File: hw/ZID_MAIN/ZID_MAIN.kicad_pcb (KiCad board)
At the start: 6 copper layers, 127 x 88.9 mm, 175 parts, among them J1 Conn 1x04 0.1" Socket, J10 FFC/FPC-40 Socket, J11 JST-PH-K B6B, J14 USB-C PWR ONLY, J15 Conn 2x03 pin hdr 0.1", J2 JST-PH-K B6B, J3 Conn 1x02 0.1" pin, J4 Conn 1x03 0.1" pin, J5 Conn 1x08 0.1" pin, J6 Conn 1x08 0.1" pin, J7 Conn 2x04 0.1" pin, J8 Conn 2x02 0.1" pin, J9 Conn 2x04 0.1" pin, M1 WS-RP2040-Zero, SW1 SW_Push, SW2 SW_DIP_x02, U1 OSC-20MHz, U10 27WZ06, U11 74LVC125AS, U12 74LVC273, U13 74FCT2245, U14 AS7C1024B, U15 ATF1508AS, U16 74FCT2245, U18 ATF1508AS, U2 74FCT2245, U20 74FCT2244, U22 ATF1504AS-44T, U23 74AHCT00, U24 74FCT2244, U3 24LC32, U4 MIC2775, U5 SST39SF010, U6 74LVC245, U7 74FCT2245, U8 74AHCT14, U9 Z80 C20MHz-PLCC

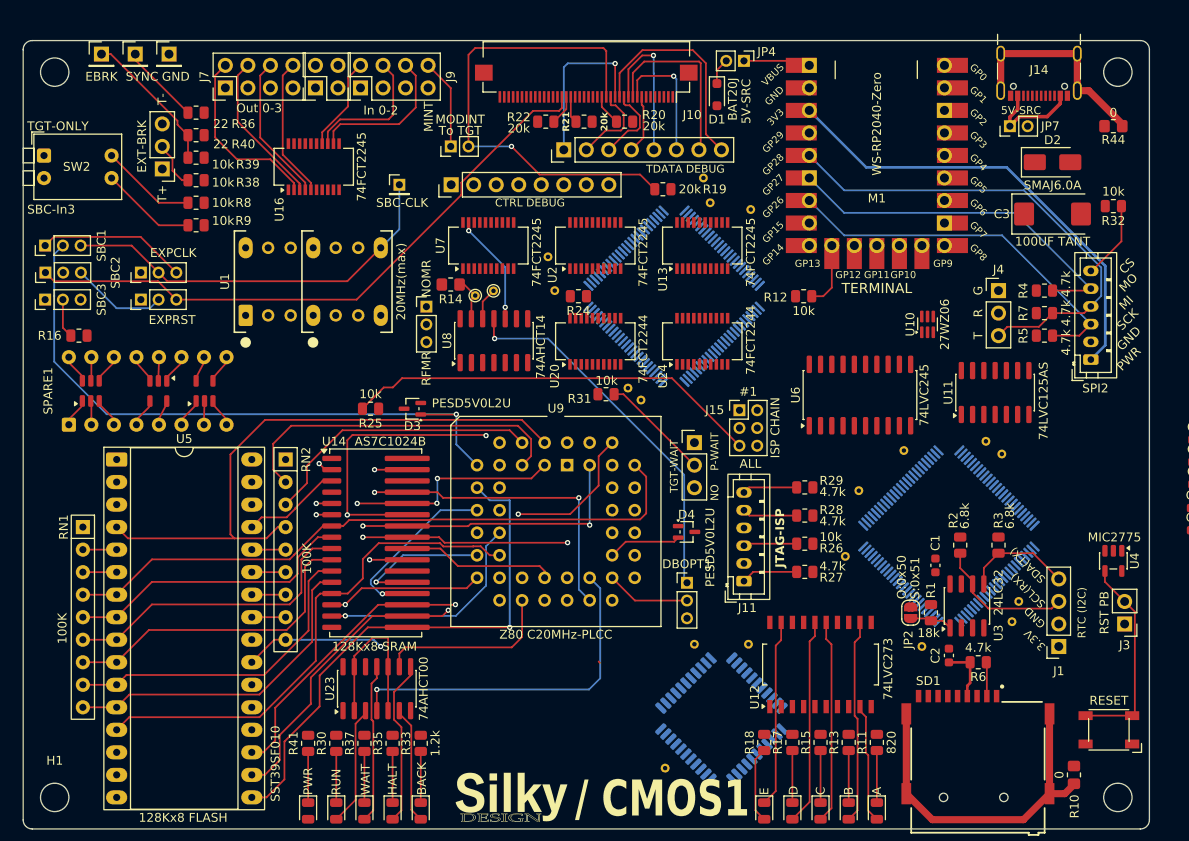
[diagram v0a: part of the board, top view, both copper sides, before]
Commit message: SCHM/PCB: Small pin assignment changes on U15.
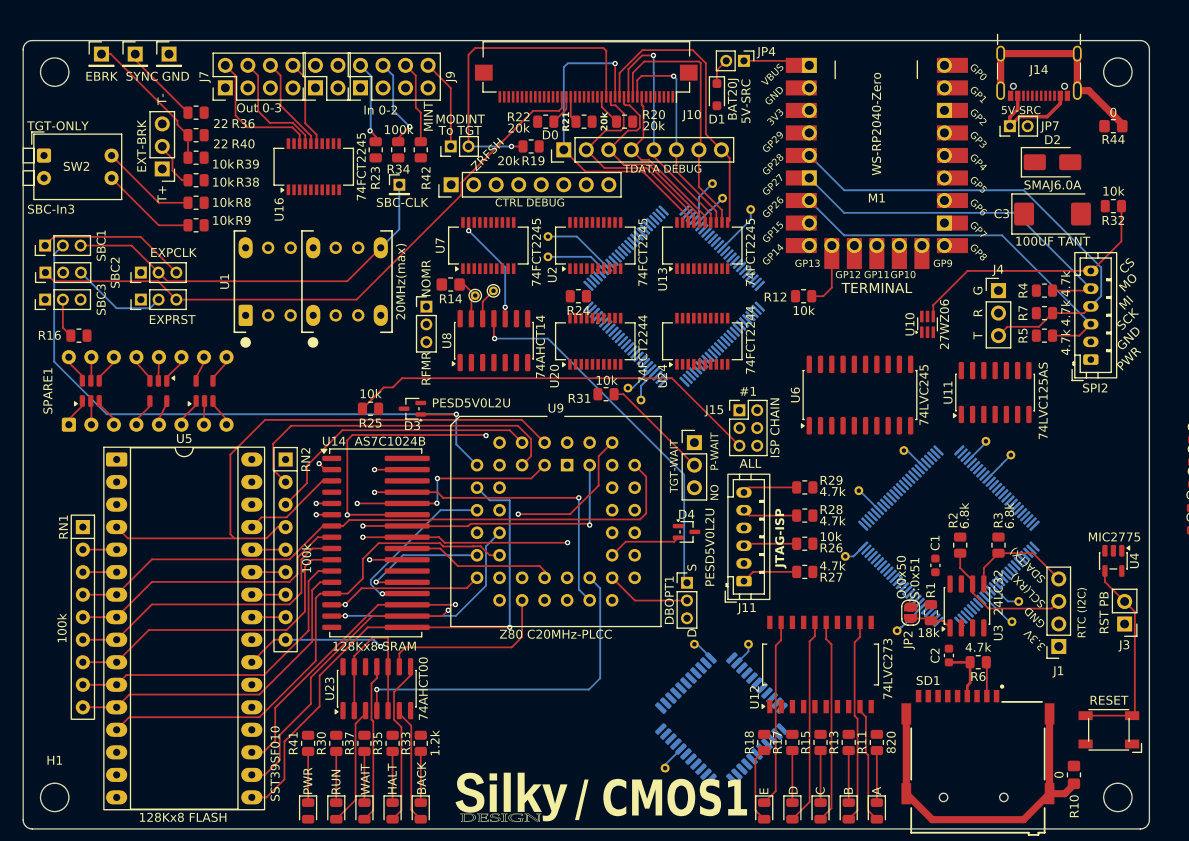
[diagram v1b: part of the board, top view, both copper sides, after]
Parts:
- added R23: 100k, Resistor_SMD:R_0805_2012Metric, F.Cu at (98.5, 68.2)
- added R34: 100k, Resistor_SMD:R_0805_2012Metric, F.Cu at (101.0, 68.2)
- added R42: 100k, Resistor_SMD:R_0805_2012Metric, F.Cu at (103.6, 68.2)
- RN1, RN2: value 100K -> 100k
- moved R19 15.6 mm to (116.0, 67.8)
- moved TP10 6.14 mm to (117.9, 78.0)
- moved TP23 3.31 mm to (157.3, 122.4)
- moved TP4 1.49 mm to (137.6, 73.7)
- moved TP5 1.20 mm to (136.5, 72.0)
- moved TP6 1.03 mm to (170.1, 102.6)
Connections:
- TP17 pad 1: Net-(U15-BMC22/IO) -> Net-(U15-BMC17/IO)
- TP19 pad 1: Net-(U15-CMC41/IO) -> Net-(U15-CMC45/IO)
- U15 pad 10: Net-(U15-BMC22/IO) -> unconnected-(U15-BMC22/IO-Pad10)
- U15 pad 14: /ZWR- -> Net-(U15-BMC17/IO)
- U15 pad 17: /ZRD- -> Net-(U15-CMC45/IO)
- U15 pad 20: Net-(U15-CMC41/IO) -> unconnected-(U15-CMC41/IO-Pad20)
- U15 pad 88: unconnected-(U15-IN/OE1-Pad88) -> /ZRD-
- U15 pad 89: unconnected-(U15-IN/GCLR-Pad89) -> /LRST-
- U15 pad 90: unconnected-(U15-IN/OE2/GCK2-Pad90) -> /ZWR-
- U16 pad 11: /ZM1- -> /TM1-
- U16 pad 12: /SBC_I2 -> /SBC_GPI2
- U16 pad 13: /SBC_I1 -> /SBC_GPI1
- U16 pad 14: /SBC_I0 -> /SBC_GPI0
- U16 pad 15: /SBC_GPO3 -> /SBC_O3
- U16 pad 16: /SBC_GPO2 -> /SBC_O2
- U16 pad 17: /SBC_GPO1 -> /SBC_O1
- U16 pad 18: /SBC_GPO0 -> /SBC_O0
- U16 pad 2: /SBC_O0 -> /SBC_GPO0
- U16 pad 3: /SBC_O1 -> /SBC_GPO1
- U16 pad 4: /SBC_O2 -> /SBC_GPO2
- U16 pad 5: /SBC_O3 -> /SBC_GPO3
- U16 pad 6: /SBC_GPI0 -> /SBC_I0
- U16 pad 7: /SBC_GPI1 -> /SBC_I1
- U16 pad 8: /SBC_GPI2 -> /SBC_I2
- U16 pad 9: /TM1- -> /ZM1-
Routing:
- net /ZA0: track 102.6 -> 37.3 mm
- net +3.3V: track 58.2 -> 6.34 mm
- net /SPICS2-: track 8.80 -> 29.3 mm
- net /TD0: track 19.0 -> 36.8 mm
- net /TINT-: track 54.5 -> 37.7 mm
- net /TD1: track 9.63 -> 25.6 mm
- net /TD2: track 9.02 -> 23.1 mm
- net /TD3: track 6.61 -> 18.8 mm
- net /TD4: track 17.2 -> 28.1 mm
- net /TD5: track 14.6 -> 24.7 mm
- net /TD6: track 20.8 -> 29.8 mm
- net /TD7: track 24.6 -> 33.3 mm
- net Net-(U18-FMC89/IO): track 0.00 -> 8.11 mm
- net /SBC_I2: track 17.0 -> 9.32 mm
- net Net-(U18-FMC88/IO): track 0.00 -> 6.95 mm
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
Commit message: PCB: AB+PCL pinout. Exp-BP add position.
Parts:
- moved TP19 10.7 mm to (160.2, 125.2)
- moved TP17 6.65 mm to (175.6, 114.3)
- moved TP6 6.03 mm to (174.1, 107.2)
- moved TP25 3.25 mm to (153.1, 116.8)
- moved TP23 1.20 mm to (156.7, 121.4)
- moved TP21 1.02 mm to (157.0, 102.2)
- moved TP24 0.53 mm to (152.7, 106.2)
- moved TP18 0.28 mm to (167.6, 101.1)
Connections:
- TP17 pad 1: Net-(U15-BMC17/IO) -> Net-(U15-BMC30/IO)
- TP19 pad 1: Net-(U15-CMC45/IO) -> Net-(U15-CMC33/IO)
- TP21 pad 1: Net-(U15-GMC107/IO) -> Net-(U15-GMC104/IO)
- TP23 pad 1: Net-(U15-DMC57/IO) -> Net-(U15-DMC54/IO)
- TP25 pad 1: Net-(U15-EMC80/IO) -> Net-(U15-EMC72/IO)
- TP6 pad 1: Net-(U15-H128/IO/GCK3) -> Net-(U15-AMC9/IO)
- U15 pad 1: /ZD2 -> /ZA5
- U15 pad 10: unconnected-(U15-BMC22/IO-Pad10) -> /ZA9
- U15 pad 100: /ZD1 -> /ZA4
- U15 pad 13: unconnected-(U15-BMC19/IO-Pad13) -> /ZA13
- U15 pad 14: Net-(U15-BMC17/IO) -> unconnected-(U15-BMC17/IO-Pad14)
- U15 pad 16: unconnected-(U15-CMC46/IO-Pad16) -> /ZD7
- U15 pad 17: Net-(U15-CMC45/IO) -> /ZD6
- U15 pad 19: unconnected-(U15-CMC43/IO-Pad19) -> /ZD5
- U15 pad 2: /ZD0 -> /ZA6
- U15 pad 20: unconnected-(U15-CMC41/IO-Pad20) -> /ZD4
- U15 pad 21: unconnected-(U15-CMC40/IO-Pad21) -> /ZD3
- U15 pad 22: unconnected-(U15-CMC38/IO-Pad22) -> /ZD2
- U15 pad 23: unconnected-(U15-CMC37/IO-Pad23) -> /ZD1
- U15 pad 24: unconnected-(U15-CMC35/IO-Pad24) -> /ZD0
- U15 pad 25: unconnected-(U15-CMC33/IO-Pad25) -> Net-(U15-CMC33/IO)
- U15 pad 28: /ZA9 -> /ZID_IO
- U15 pad 31: Net-(U15-DMC57/IO) -> unconnected-(U15-DMC57/IO-Pad31)
- U15 pad 33: unconnected-(U15-DMC54/IO-Pad33) -> Net-(U15-DMC54/IO)
- U15 pad 40: /ZA10 -> unconnected-(U15-EMC65/IO-Pad40)
- U15 pad 41: /ZA11 -> unconnected-(U15-E67/IO/PD2-Pad41)
- U15 pad 42: /ZA12 -> unconnected-(U15-EMC69/IO-Pad42)
- U15 pad 44: /ZA13 -> unconnected-(U15-EMC70/IO-Pad44)
- U15 pad 45: /ZA14 -> Net-(U15-EMC72/IO)
- U15 pad 47: /ZA8 -> /ZA12
- U15 pad 48: /ZA4 -> unconnected-(U15-EMC77/IO-Pad48)
- U15 pad 49: /ZA5 -> /ZA14
- U15 pad 5: /ZA3 -> Net-(U15-BMC30/IO)
- U15 pad 50: Net-(U15-EMC80/IO) -> unconnected-(U15-EMC80/IO-Pad50)
- U15 pad 52: /ZA6 -> unconnected-(U15-FMC81/IO-Pad52)
- U15 pad 53: /ZA7 -> unconnected-(U15-FMC83/IO-Pad53)
- U15 pad 57: unconnected-(U15-FMC89/IO-Pad57) -> /ZA10
- U15 pad 60: unconnected-(U15-FMC93/IO-Pad60) -> /ZA8
- U15 pad 68: /ZID_IO -> Net-(U15-GMC104/IO)
- U15 pad 7: /BRKN_AEQ -> /ZA1
- U15 pad 70: Net-(U15-GMC107/IO) -> unconnected-(U15-GMC107/IO-Pad70)
- U15 pad 8: /BRK1_AEQ -> unconnected-(U15-BMC25/IO-Pad8)
- U15 pad 85: Net-(U15-H128/IO/GCK3) -> unconnected-(U15-H128/IO/GCK3-Pad85)
- U15 pad 9: unconnected-(U15-BMC24/IO-Pad9) -> /ZA3
- U15 pad 92: /ZD7 -> /BRKN_AEQ
- U15 pad 93: /ZA1 -> /BRK1_AEQ
- U15 pad 94: /ZA0 -> unconnected-(U15-AMC13/IO-Pad94)
- U15 pad 96: /ZD6 -> /ZA0
- U15 pad 97: /ZD4 -> Net-(U15-AMC9/IO)
- U15 pad 98: /ZD5 -> /ZA11
- U15 pad 99: /ZD3 -> /ZA7
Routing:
- net Net-(U15-BMC30/IO): track 0.00 -> 5.76 mm
- net Net-(U15-CMC33/IO): track 0.00 -> 5.67 mm
- net Net-(U15-CMC45/IO): track 4.28 -> 0.00 mm
- net Net-(U15-DMC57/IO): track 4.09 -> 0.00 mm
- net Net-(U15-DMC54/IO): track 0.00 -> 3.85 mm
- net Net-(U15-H128/IO/GCK3): track 3.75 -> 0.00 mm
- net Net-(U15-BMC17/IO): track 3.47 -> 0.00 mm
- net Net-(U15-GMC104/IO): track 0.00 -> 3.41 mm
- net Net-(U15-AMC9/IO): track 0.00 -> 3.30 mm
- net Net-(U15-EMC72/IO): track 0.00 -> 3.02 mm
- net Net-(U15-GMC107/IO): track 2.49 -> 0.00 mm
- net Net-(U15-EMC80/IO): track 2.48 -> 0.00 mm
- net Net-(U15-FMC88/IO): track 3.09 -> 3.69 mm

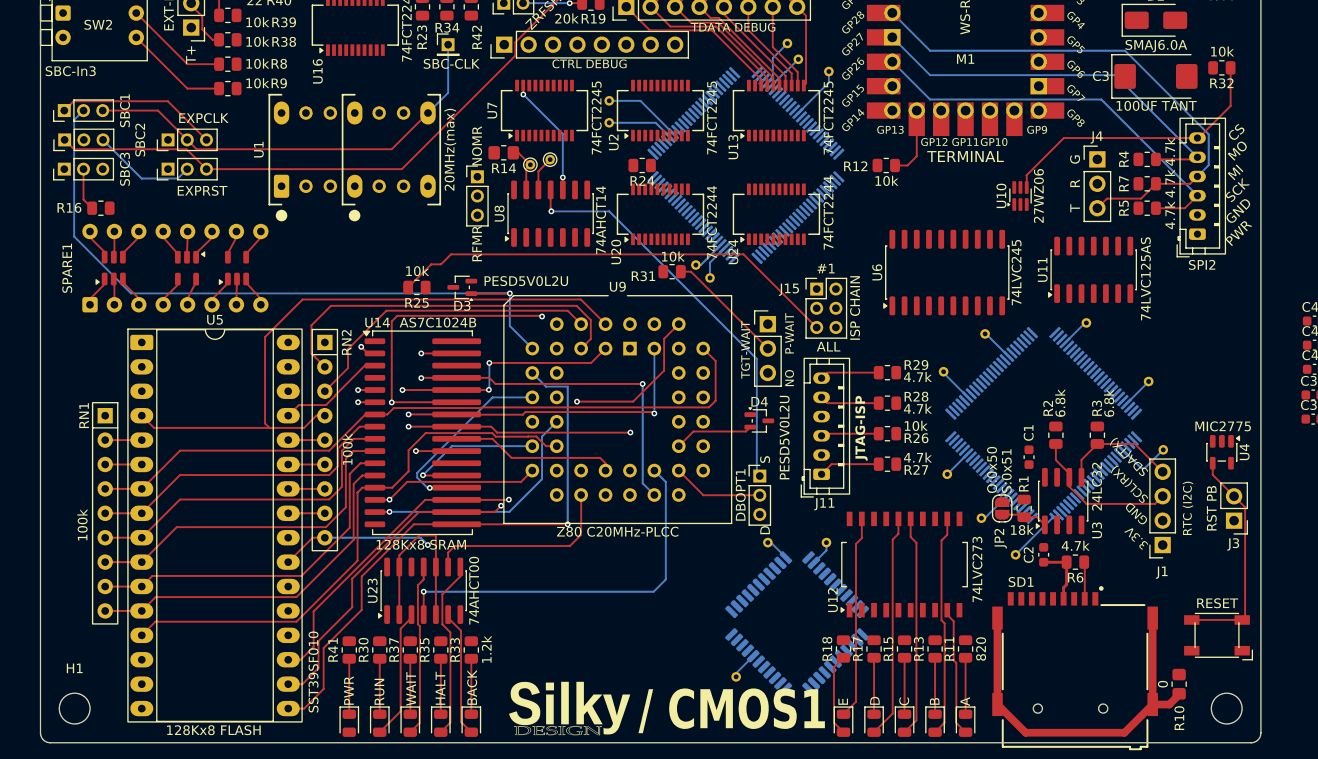
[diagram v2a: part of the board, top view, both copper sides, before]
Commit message: PCB layout progress before SRAM move. PLD: Allow upper-8 address only on BRK1.
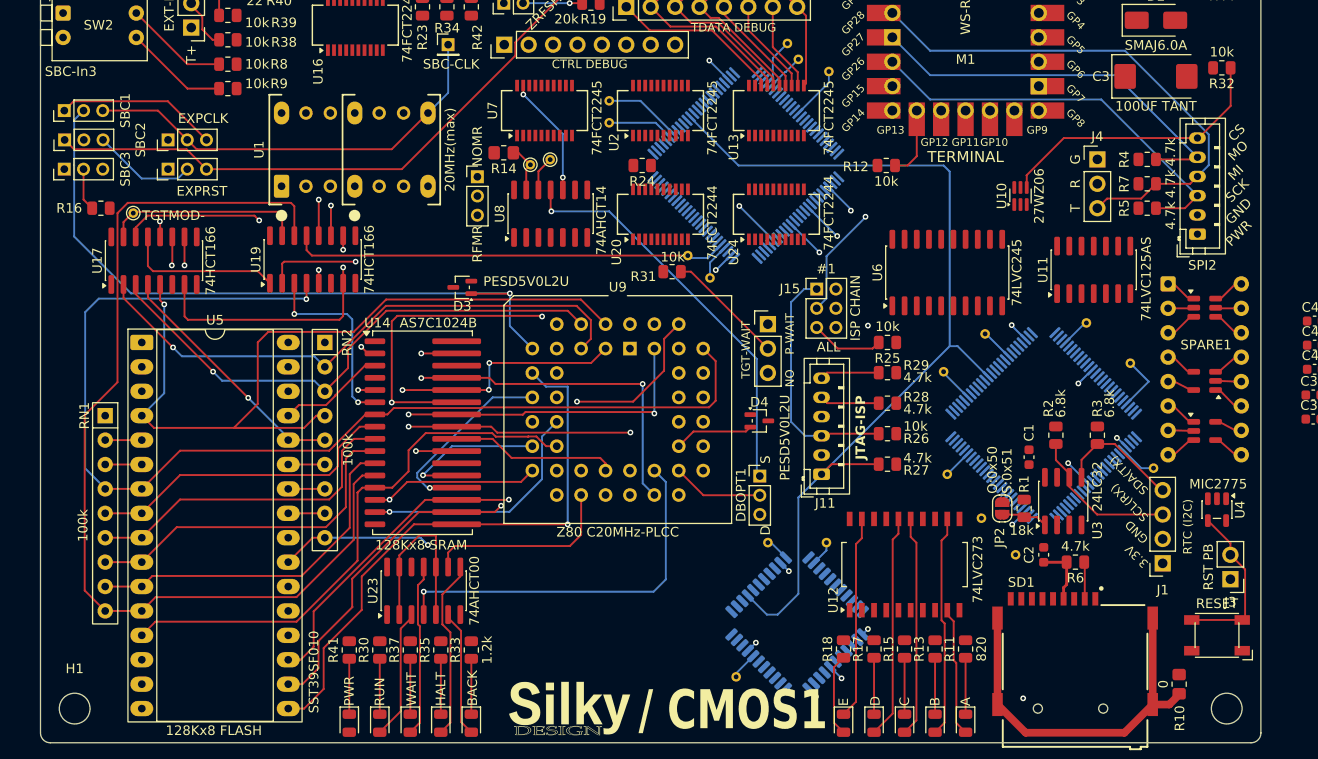
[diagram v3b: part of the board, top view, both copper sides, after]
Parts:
- added TP12: TestPoint, TestPoint:TestPoint_THTPad_D1.0mm_Drill0.5mm, F.Cu at (68.4, 89.7)
- added U17: 74HCT166, Package_SO:SOIC-16_3.9x9.9mm_P1.27mm, F.Cu at (70.5, 94.6)
- added U19: 74HCT166, Package_SO:SOIC-16_3.9x9.9mm_P1.27mm, F.Cu at (87.1, 94.5)
- moved SPARE1 112.2 mm to (176.1, 97.0), turned to 0 degrees
- moved R25 49.3 mm to (146.9, 103.1)
- moved J3 6.10 mm to (182.6, 127.8)
- moved U4 5.99 mm to (181.2, 120.5)
- moved TP6 2.69 mm to (172.1, 105.3)
- moved TP17 2.16 mm to (174.6, 116.2)
- moved J1 1.91 mm to (175.5, 126.1)
- moved TP9 1.30 mm to (126.1, 94.1)
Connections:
- net /IO59 renamed /PCRD_DIN
- TP19 pad 1: Net-(U15-CMC33/IO) -> Net-(U15-DMC54/IO)
- TP23 pad 1: Net-(U15-DMC54/IO) -> Net-(U15-CMC33/IO)
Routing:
- net /PC_LATCH-: track 0.00 -> 119.5 mm, vias 0 -> 3
- net /ZID_IO: track 0.00 -> 99.4 mm, vias 0 -> 5
- net /JTCK: track 6.38 -> 98.5 mm
- net /JTMS: track 6.20 -> 89.9 mm, vias 0 -> 3
- net /ZA1: track 105.1 -> 176.3 mm, vias 0 -> 1
- net /ZA2: track 100.0 -> 168.4 mm, vias 0 -> 1
- net /ZA0: track 37.3 -> 103.1 mm
- net /ZA3: track 100.0 -> 160.1 mm, vias 0 -> 1
- net /ZA10: track 81.2 -> 136.7 mm, vias 2 -> 3
- net /ZA4: track 94.8 -> 147.9 mm, vias 0 -> 1
- net /TGT_NOW: track 0.00 -> 52.9 mm, vias 0 -> 2
- net /JTD2O3I: track 0.00 -> 49.4 mm, vias 0 -> 3
- net /ZA5: track 73.3 -> 117.8 mm, vias 0 -> 1
- net /PCRD_DIN: track 3.49 -> 45.5 mm
- net /ZA8: track 56.2 -> 97.4 mm, vias 2 -> 3
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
